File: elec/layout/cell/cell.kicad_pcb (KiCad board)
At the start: 4 copper layers, 65 parts, among them Q1 ?, Q2 ?, Q3 ?, U1 ?, U10 ?, U11 ?, U12 ?, U13 ?, U14 ?, U2 ?, U3 ?, U4 ?, U5 ?, U6 ?, U7 ?, U8 ?, U9 ?

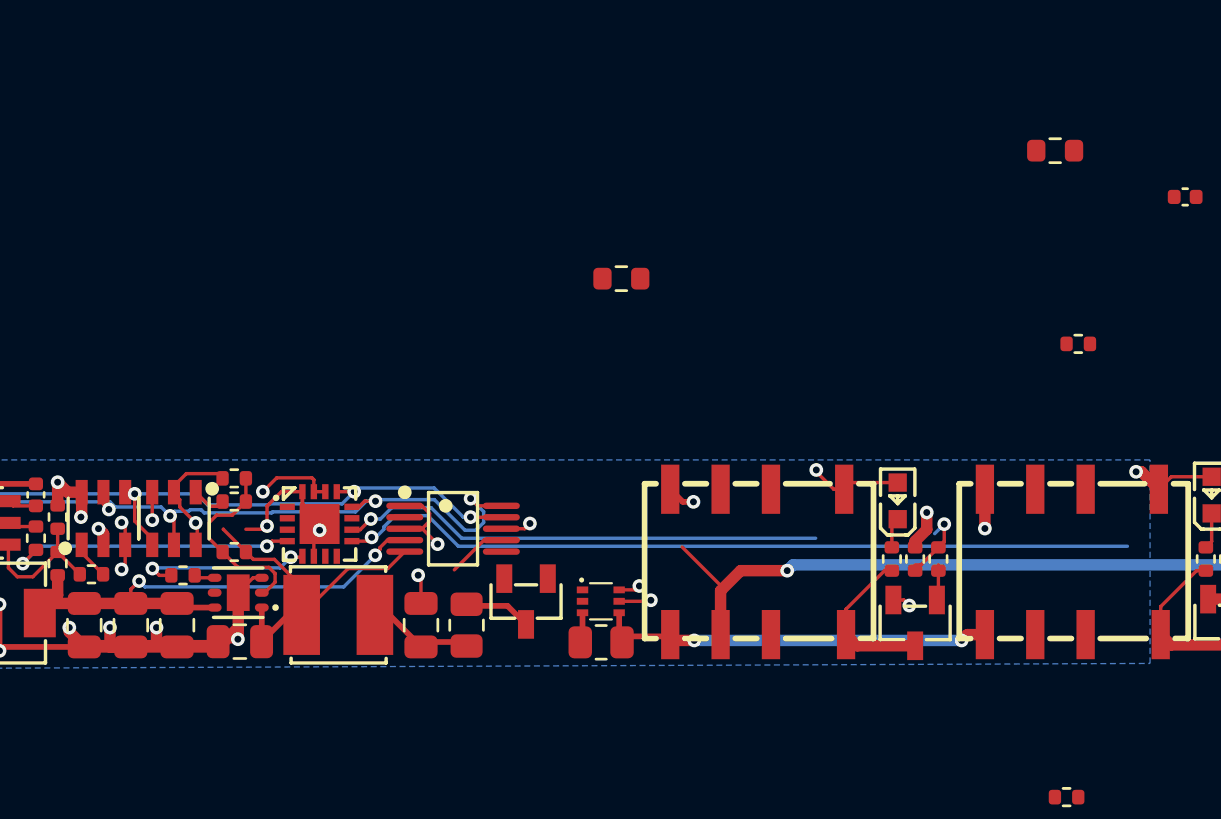
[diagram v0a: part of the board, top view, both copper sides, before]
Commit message: cleanup net names
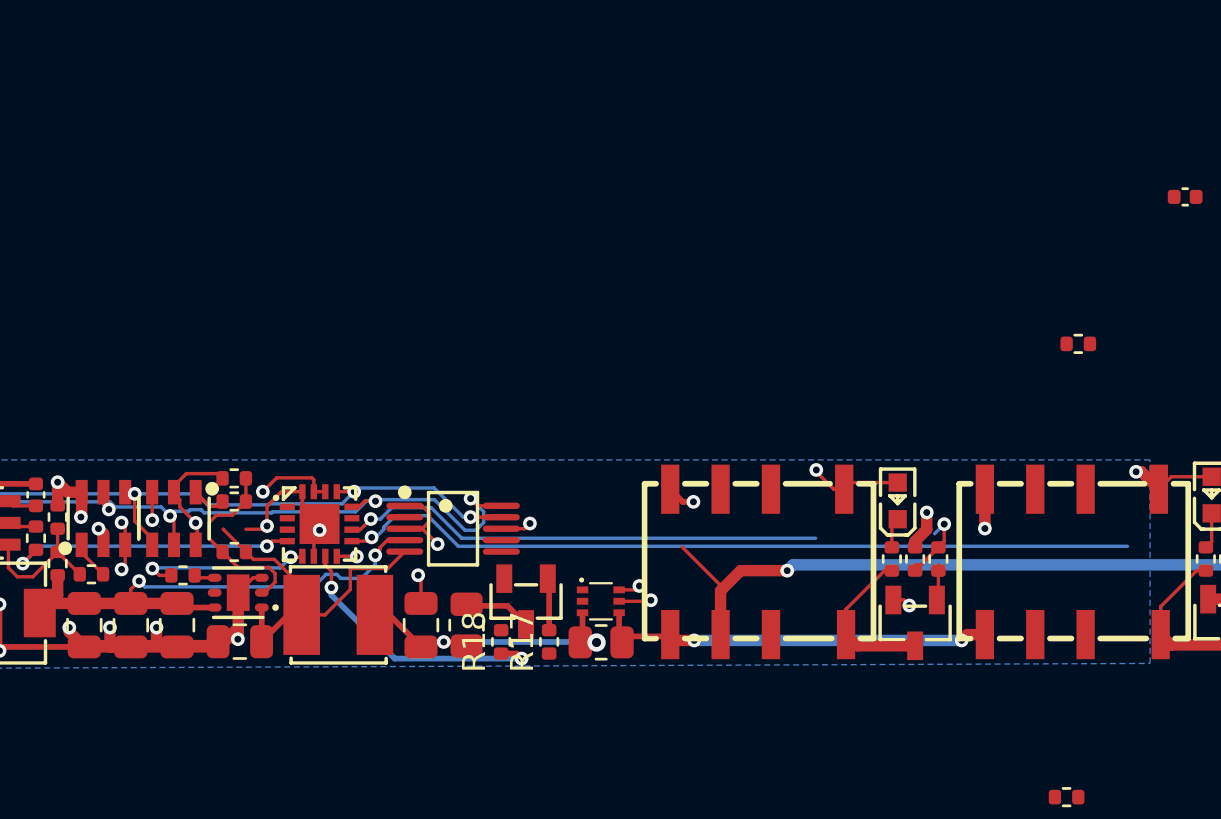
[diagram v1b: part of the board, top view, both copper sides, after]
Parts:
- R17: value 100mW Thick Film Resistors 75V ±100ppm/℃ ±1% 1kΩ 0603 Chip Resistor - Surface Mount ROHS -> 62.5mW Thick Film Resistors 50V ±100ppm/℃ ±1% 1kΩ 0402 Chip Resistor - Surface Mount ROHS; footprint lib:R0603 -> lib:R0402
- R18: value 100mW Thick Film Resistors 75V ±100ppm/℃ ±1% 10kΩ 0603 Chip Resistor - Surface Mount ROHS -> 62.5mW Thick Film Resistors 50V ±100ppm/℃ ±1% 10kΩ 0402 Chip Resistor - Surface Mount ROHS; footprint lib:R0603 -> lib:R0402
- moved R18 32.3 mm to (117.7, 123.8), turned to 90 degrees
- moved R17 16.2 mm to (119.8, 123.8), turned to 90 degrees
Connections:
- U10 pad 8: p5 -> input
- U10 pad 9: p6 -> dmm_relay_enable
- U2 pad 8: vcc-7 -> vcc-6
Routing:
- net p6: track 35.0 -> 0.00 mm, vias 1 -> 0
- net dmm_relay_enable: track 3.03 -> 38.0 mm, vias 1 -> 2
- net p4: track 0.00 -> 12.3 mm, vias 0 -> 2
- net vcc-5: track 5.77 -> 13.2 mm, vias 0 -> 2
- net load_switch.fet-gate: track 0.00 -> 2.32 mm
- net ain3: track 2.59 -> 0.76 mm
- net vcc-6: track 87.6 -> 89.0 mm, vias 3 -> 4
- net vcc-7: track 16.0 -> 14.7 mm, vias 9 -> 8
- net input: track 3.04 -> 3.92 mm, vias 1 -> 2
- net adc-vcc-1: track 16.6 -> 17.1 mm

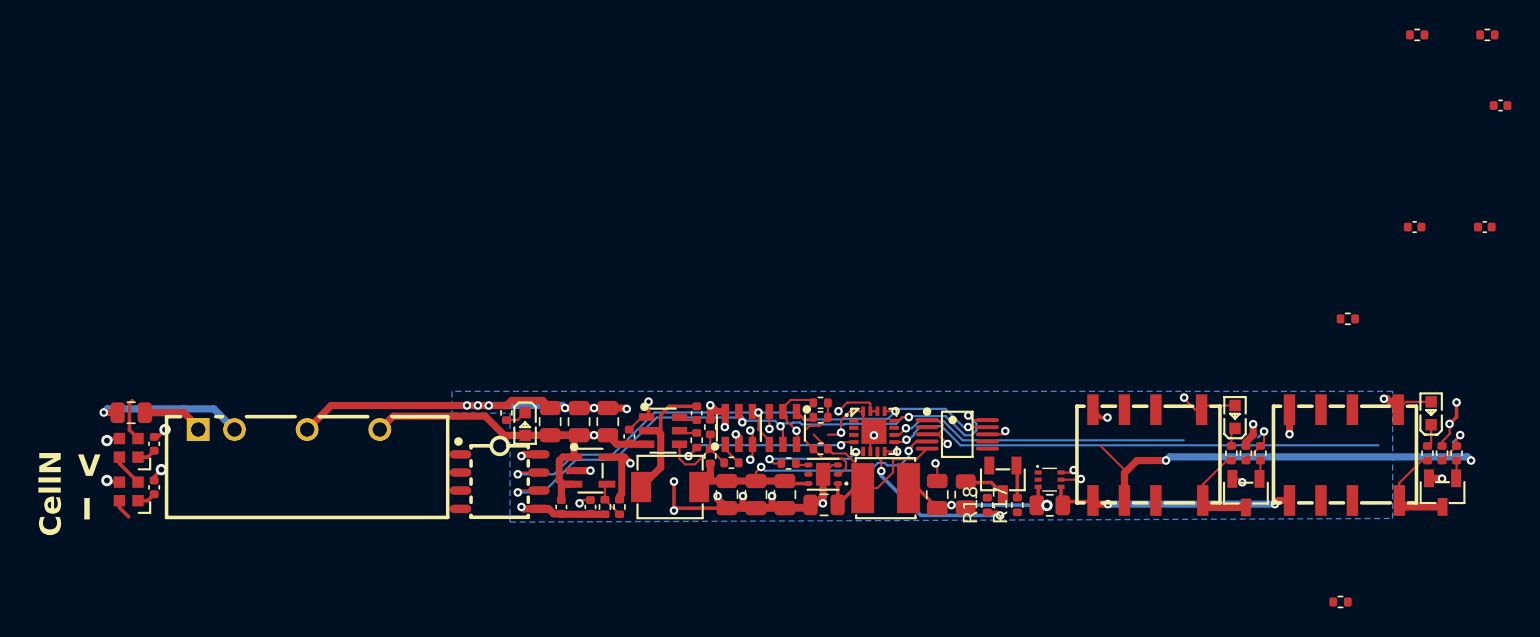
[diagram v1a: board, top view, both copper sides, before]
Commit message: add library parts
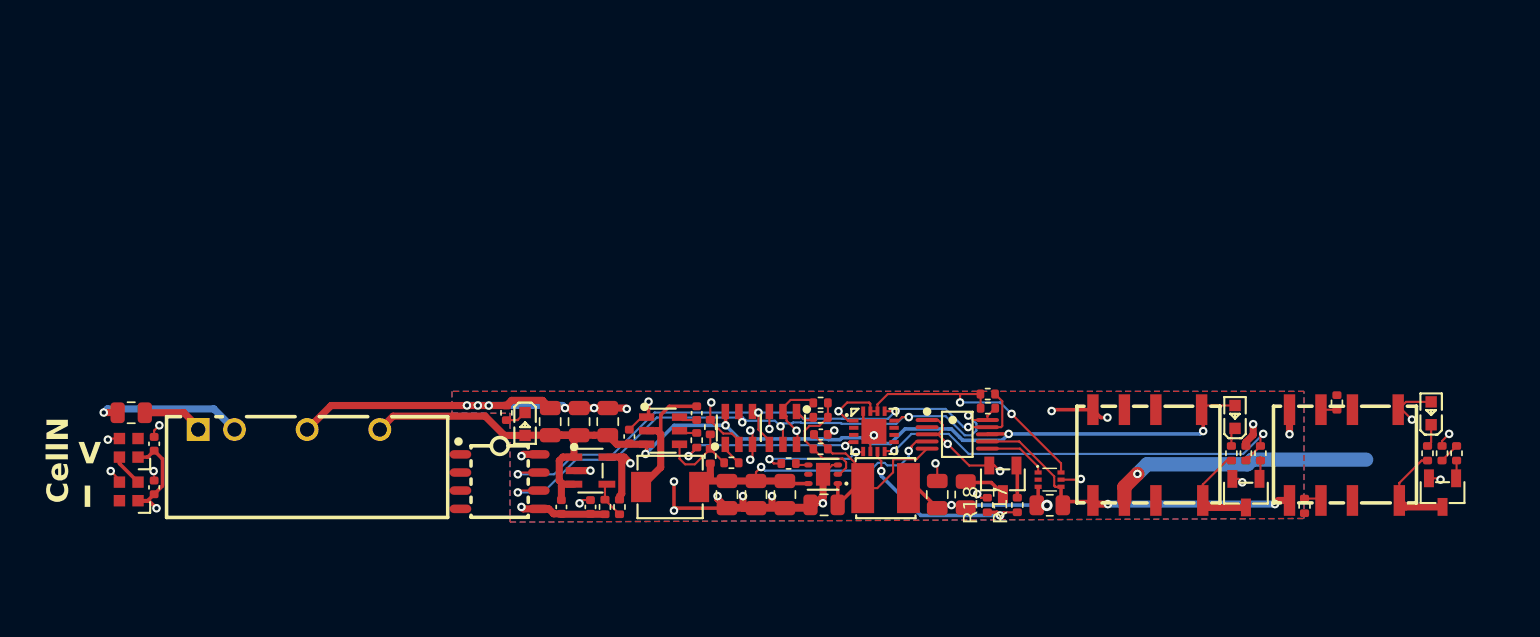
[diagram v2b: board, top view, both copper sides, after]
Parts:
- removed the C11 at (152.5, 104.3)
- removed the C12 at (147.6, 104.3)
- moved C10 52.8 mm to (106.1, 118.8)
- moved R21 43.6 mm to (117.7, 117.0), turned to 180 degrees
- moved R20 39.1 mm to (117.7, 116.0), turned to 180 degrees
- moved R24 7.18 mm to (139.9, 123.8), turned to -90 degrees
- moved R25 5.89 mm to (142.2, 116.6), turned to 90 degrees
- renumbered C13 to C11, C14 to C12, C15 to C13, C16 to C14, C17 to C15, C18 to C16
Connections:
- R10 pad 2: current_sense.sensor-vcc -> adc-vcc-2
- U10 pad 9: dmm_relay_enable -> p6
- U2 pad 6: vcc-1 -> ain2
- U2 pad 7: ain3 -> adc-vcc-2
- U7 pad 1: ain3 -> ain2
- U7 pad 4: current_sense.sensor-vcc -> adc-vcc-2
- U8 pad 5: current_sense.sensor-vcc -> adc-vcc-2
- U9 pad 5: current_sense.sensor-vcc -> adc-vcc-2
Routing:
- net dmm_relay_enable: track 38.0 -> 1.44 mm, vias 2 -> 0
- net input: track 3.92 -> 30.4 mm
- net adc-vcc-2: track 0.00 -> 24.3 mm, vias 0 -> 2
- net p7: track 21.4 -> 0.00 mm, vias 1 -> 0
- net vcc-7: track 14.7 -> 34.1 mm, vias 8 -> 9
- net current_sense.sensor-vcc: track 17.5 -> 0.00 mm, vias 2 -> 0
- net vcc-1: track 31.3 -> 18.6 mm, vias 2 -> 1
- net vcc-6: track 89.0 -> 77.2 mm
- net vcc-2: track 2.63 -> 11.5 mm, vias 0 -> 2
- net gnd-6: track 100.9 -> 105.4 mm
- net ain2: track 0.00 -> 4.47 mm
- net sda-1: track 40.5 -> 44.0 mm
- net led_data: track 2.99 -> 0.00 mm
- net gnd-2: track 8.19 -> 5.40 mm
- net adc-vcc-1: track 17.1 -> 15.6 mm
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- added copper zone on F.Cu, net gnd-6
- added copper zone on In2.Cu, net gnd-6
